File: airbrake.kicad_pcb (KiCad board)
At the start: 2 copper layers, 53.9 x 52.1 mm, 76 parts, among them IC1 SN74HCT125DR, J1 Molex Microfit, J2 Molex Microfit, J3 Molex Microfit, J4 Molex Microfit, J5 Molex Microfit, J6 Conn_02x03_Counter_Clockwise, U1 MS560702BA03-50, U2 MMC5983MA, U3 STM32G431RBTx, U4 TMP275AIDGKR, U5 LP5912Q3.3DRVRQ1, U6 BMI088, U7 TPS62153, U8 USBLC6-2SC6, U9 W25Q256JVEIQTR, X1 ECS-TXO-32CSMV-320-AN-TR

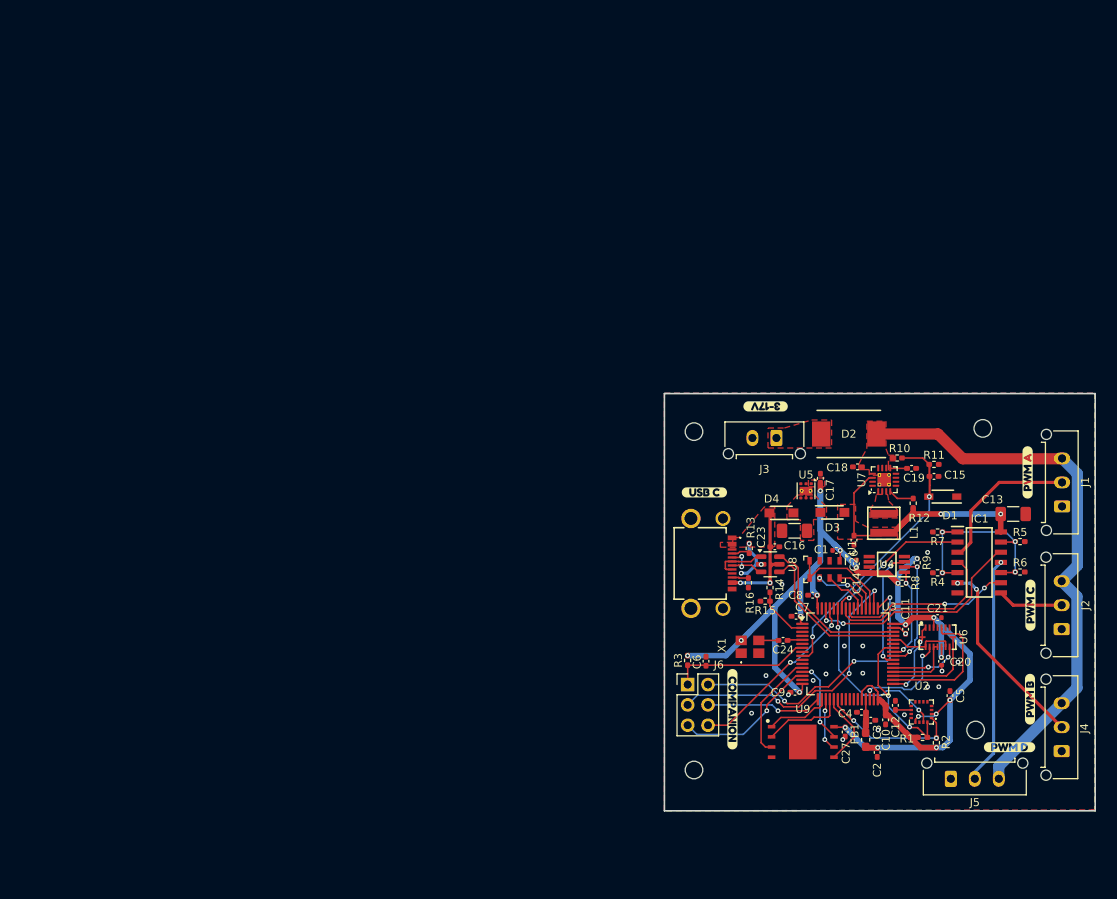
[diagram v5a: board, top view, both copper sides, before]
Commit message: feat: v2 schematic
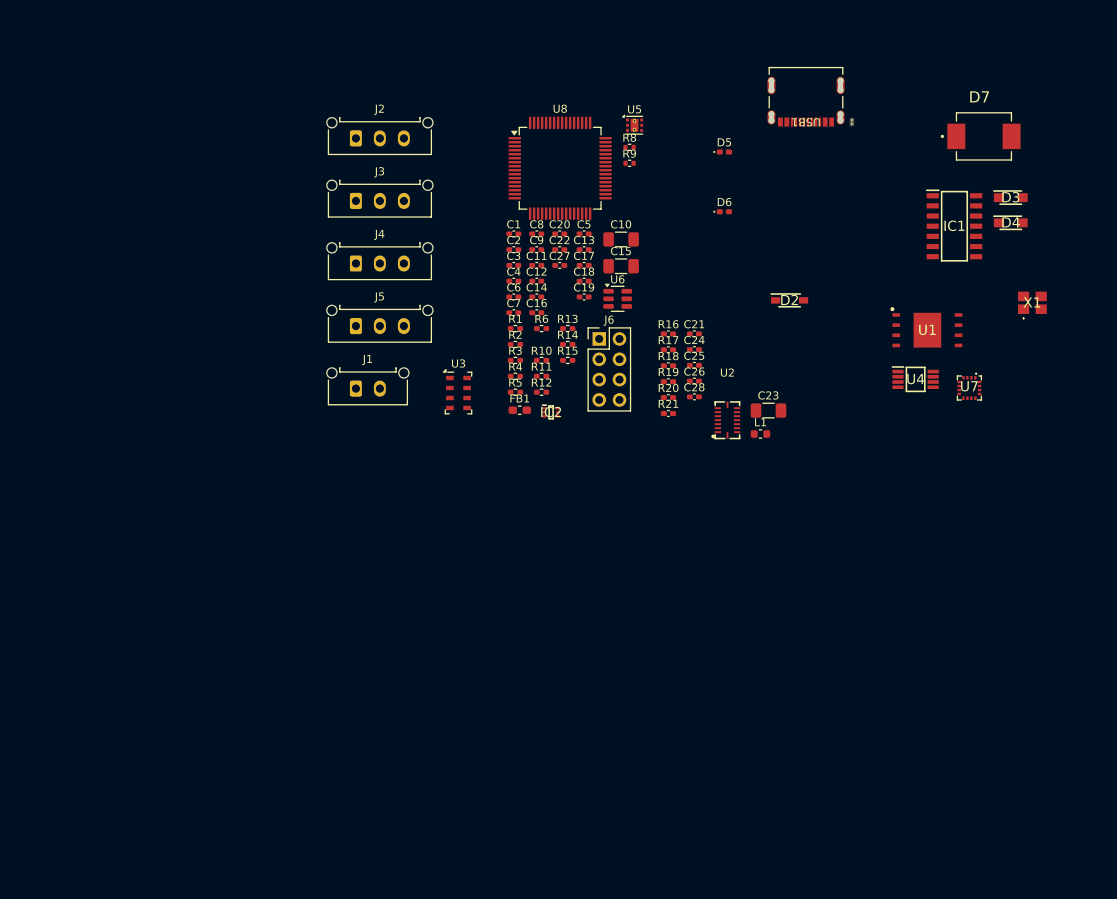
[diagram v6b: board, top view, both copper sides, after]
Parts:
- removed D1: MMSZ4683T1G, SamacSys:SOD3716X135N
- removed H1, H2, H3, H4: MountingHole, MountingHole:MountingHole_2.2mm_M2
- removed R7: 470R, Resistor_SMD:R_0402_1005Metric_Pad0.72x0.64mm_HandSolder
- removed U9: W25Q256JVEIQTR, SamacSys:SON127P800X600X80-9N-D
- removed kibuzzard-67AC9DCF: G***, kibuzzard-67AC9DCF
- removed kibuzzard-67AC9E05: G***, kibuzzard-67AC9E05
- removed kibuzzard-67AC9E3B: G***, kibuzzard-67AC9E3B
- removed kibuzzard-67AC9E4A: G***, kibuzzard-67AC9E4A
- removed kibuzzard-67AC9E5D: G***, kibuzzard-67AC9E5D
- removed kibuzzard-67AC9E80: G***, kibuzzard-67AC9E80
- removed kibuzzard-67B37024: G***, kibuzzard-67B37024
- added C22: 10uF, Capacitor_SMD:C_0402_1005Metric_Pad0.74x0.62mm_HandSolder, F.Cu at (110.6, 61.5)
- added C25: 10uF, Capacitor_SMD:C_0402_1005Metric_Pad0.74x0.62mm_HandSolder, F.Cu at (127.5, 75.9)
- added C28: 10nF, Capacitor_SMD:C_0402_1005Metric_Pad0.74x0.62mm_HandSolder, F.Cu at (127.5, 79.9)
- added D5: PWR_LED, LED_SMD:LED_0402_1005Metric_Pad0.77x0.64mm_HandSolder, F.Cu at (131.2, 49.2)
- added D6: USB_LED, LED_SMD:LED_0402_1005Metric_Pad0.77x0.64mm_HandSolder, F.Cu at (131.2, 56.7)
- added D7: SS34, footprints:DIOM7959X265N, F.Cu at (163.6, 47.3)
- added IC2: TPS563203DRLR, footprints:SOTFL50P160X60-6N, F.Cu at (109.5, 81.8)
- added R17: 10k, Inductor_SMD:L_0402_1005Metric_Pad0.77x0.64mm_HandSolder, F.Cu at (124.2, 74.0)
- added R18: 10k, Inductor_SMD:L_0402_1005Metric_Pad0.77x0.64mm_HandSolder, F.Cu at (124.2, 76.0)
- added R19: 22k, Inductor_SMD:L_0402_1005Metric_Pad0.77x0.64mm_HandSolder, F.Cu at (124.2, 78.0)
- added R20: 100k, Inductor_SMD:L_0402_1005Metric_Pad0.77x0.64mm_HandSolder, F.Cu at (124.2, 80.0)
- added R21: 100k, Inductor_SMD:L_0402_1005Metric_Pad0.77x0.64mm_HandSolder, F.Cu at (124.2, 81.9)
- C1, C14, C20: footprint Capacitor_SMD:C_0402_1005Metric -> Capacitor_SMD:C_0402_1005Metric_Pad0.74x0.62mm_HandSolder
- C10, C15: value 100nF -> 100uF; footprint Capacitor_SMD:C_0402_1005Metric_Pad0.74x0.62mm_HandSolder -> Capacitor_SMD:C_1206_3216Metric_Pad1.33x1.80mm_HandSolder
- C12: value 10uF -> 100nF
- C13: value 100uF -> 100nF; footprint Capacitor_SMD:C_1206_3216Metric_Pad1.33x1.80mm_HandSolder -> Capacitor_SMD:C_0402_1005Metric_Pad0.74x0.62mm_HandSolder
- C16: value 100uF -> 1uF; footprint Capacitor_SMD:C_1206_3216Metric_Pad1.33x1.80mm_HandSolder -> Capacitor_SMD:C_0402_1005Metric_Pad0.74x0.62mm_HandSolder
- C17: value 2.2uF -> 10uF
- C18: value 10uF -> 2.2uF
- C19: value 3.3pF -> 10nF
- C21: value 100nF -> 22uF; footprint Capacitor_SMD:C_0402_1005Metric -> Capacitor_SMD:C_0402_1005Metric_Pad0.74x0.62mm_HandSolder
- C23: value 10uF -> 100uF; footprint Capacitor_SMD:C_0402_1005Metric_Pad0.74x0.62mm_HandSolder -> Capacitor_SMD:C_1206_3216Metric_Pad1.33x1.80mm_HandSolder
- C24: value 10nF -> 22uF
- C26: value 22uF -> 100nF
- C3: value 10nF -> 100nF
- C4, C5: value 1uF -> 100nF
- C6: value 100nF -> 10nF
- C8: value 100nF -> 1uF
- D2: value SS34 -> MMSZ4683T1G; footprint SamacSys:DIOM7959X262N -> footprints:SOD3716X135N
- D3, D4: footprint SamacSys:SODFL3616X98N -> footprints:SODFL3616X98N
- IC1: footprint SamacSys:SOIC127P600X175-14N -> footprints:SOIC127P600X175-14N
- J1: footprint Connector_Molex:Molex_Micro-Fit_3.0_43650-0315_1x03_P3.00mm_Vertical -> Connector_Molex:Molex_Micro-Fit_3.0_43650-0215_1x02_P3.00mm_Vertical
- J3: footprint Connector_Molex:Molex_Micro-Fit_3.0_43650-0215_1x02_P3.00mm_Vertical -> Connector_Molex:Molex_Micro-Fit_3.0_43650-0315_1x03_P3.00mm_Vertical
- J6: footprint Connector_PinHeader_2.54mm:PinHeader_2x03_P2.54mm_Vertical -> Connector_PinHeader_2.54mm:PinHeader_2x04_P2.54mm_Vertical
- L1: value 2.2uH -> 4.7uH; footprint SamacSys:XFL4020472MEC -> Inductor_SMD:L_0603_1608Metric
- R1: value 4.7k -> 10k
- R10, R14: value 10k -> 4.7k
- R11: value 47k -> 5.1k
- R12: value 100k -> 10k
- R13: value 5.1k -> 22k
- R15: value 22k -> 10k
- R16: value 5.1k -> 100k; footprint Resistor_SMD:R_0402_1005Metric_Pad0.72x0.64mm_HandSolder -> Inductor_SMD:L_0402_1005Metric_Pad0.77x0.64mm_HandSolder
- R2: value 4.7k -> 47k
- R3: value 10k -> 470R
- U1: value MS560702BA03-50 -> W25Q256JVEIQTR; footprint Package_LGA:LGA-8_3x5mm_P1.25mm -> footprints:SON127P800X600X80-9N-D
- U2: value MMC5983MA -> BMI088; footprint SamacSys:MMC5983MA -> footprints:LGA-16_L4.5-W3.0-P0.50-BL
- U3: value STM32G431RBTx -> MS560702BA03-50; footprint Package_QFP:LQFP-64_10x10mm_P0.5mm -> Package_LGA:LGA-8_3x5mm_P1.25mm
- U4: footprint SamacSys:SOP65P490X110-8N -> footprints:SOP65P490X110-8N
- U6: value BMI088 -> USBLC6-2SC6; footprint EasyEDA:LGA-16_L4.5-W3.0-P0.50-BL -> Package_TO_SOT_SMD:SOT-23-6
- U7: value TPS62153 -> MMC5983MA; footprint Package_DFN_QFN:VQFN-16-1EP_3x3mm_P0.5mm_EP1.68x1.68mm_ThermalVias -> footprints:MMC5983MA
- U8: value USBLC6-2SC6 -> STM32G431RBTx; footprint Package_TO_SOT_SMD:SOT-23-6 -> Package_QFP:LQFP-64_10x10mm_P0.5mm
- USB1: value 10172013-00011LF -> 2137160001; footprint SamacSys:1017201300011LF -> footprints:2171790001_MOL
- X1: footprint SamacSys:ECSTXO32CSMV320ANTR -> footprints:ECSTXO32CSMV320ANTR
- moved J2 107.5 mm to (85.1, 47.5), turned to 0 degrees
- moved J4 107.2 mm to (85.1, 63.2), turned to 0 degrees
- moved J5 93.4 mm to (85.1, 71.0)
- moved J1 89.5 mm to (85.1, 78.8), turned to 0 degrees
- moved C2 77.5 mm to (104.9, 61.5), turned to 0 degrees
- moved C5 73.6 mm to (113.7, 59.5), turned to 0 degrees
- moved R2 72.4 mm to (105.1, 73.3), turned to 0 degrees
- moved C3 72.3 mm to (104.9, 63.4)
- moved R1 72.1 mm to (105.1, 71.3), turned to 0 degrees
- moved C20 71.6 mm to (110.6, 59.5), turned to 0 degrees
- moved C12 69.4 mm to (107.7, 65.4), turned to 0 degrees
- moved C4 69.2 mm to (104.9, 65.4), turned to 0 degrees
- moved C10 68.6 mm to (118.3, 60.2), turned to 0 degrees
- moved C27 68.4 mm to (110.6, 63.4), turned to 0 degrees
- moved R6 67.1 mm to (108.3, 71.3)
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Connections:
- C1 pad 1: VBAT- -> +3.3V
- C1 pad 2: +3.3V -> VBAT-
- C10 pad 1: +3.3V -> 6V0
- C12 pad 1: Net-(U2-CAP) -> +3.3V
- C13 pad 1: +5V -> +3.3V
- C15 pad 1: VBAT- -> Net-(D3-K)
- C15 pad 2: BAT_LEVEL -> VBAT-
- C16 pad 1: Net-(D3-K) -> VBAT-
- C16 pad 2: VBAT- -> +3.3V
- C17 pad 2: +3.3V -> VBUS
- C18 pad 2: VBAT+ -> +3.3V
- C19 pad 1: VBAT- -> HSE_IN
- C19 pad 2: Net-(U7-SS/TR) -> Net-(X1-OUTPUT)
- C20 pad 1: +3.3V -> VBAT-
- C20 pad 2: VBAT- -> +3.3V
- C21 pad 1: +3.3V -> 6V0
- C23 pad 1: VBAT- -> VBAT+
- C23 pad 2: VBUS -> VBAT-
- C24 pad 1: HSE_IN -> 6V0
- C24 pad 2: Net-(X1-OUTPUT) -> VBAT-
- C26 pad 1: VBAT- -> Net-(IC2-SW)
- C26 pad 2: +5V -> Net-(IC2-BST)
- C27 pad 1: +3.3V -> VBAT-
- C27 pad 2: VBAT- -> nRST
- C3 pad 1: +3.3VA -> +3.3V
- C4 pad 1: +3.3VA -> +3.3V
- C5 pad 2: +3.3V -> BAT_LEVEL
- C6 pad 1: VBAT- -> +3.3VA
- C6 pad 2: nRST -> VBAT-
- C8 pad 1: +3.3V -> +3.3VA
- D2 pad 1: VBAT+ -> VBAT-
- D2 pad 2: Net-(D2-A) -> BAT_LEVEL
- D3 pad 2: +5V -> 6V0
- IC1 pad 14: +5V -> 6V0
- J1 pad 1: VBAT- -> Net-(J1-Pin_1)
- J1 pad 2: SERVO_A -> VBAT-
- J2 pad 2: SERVO_C -> SERVO_A
- J2 pad 3: VBAT+ -> 6V0
- J3 pad 1: Net-(D2-A) -> VBAT-
- J3 pad 2: VBAT- -> SERVO_B
- J4 pad 2: SERVO_B -> SERVO_C
- J4 pad 3: VBAT+ -> 6V0
- J5 pad 3: VBAT+ -> 6V0
- J6 pad 1: nRST -> VBAT-
- J6 pad 4: COMPANION_RX -> +3.3V
- J6 pad 5: COMPANION_TX -> COMPANION_RX
- J6 pad 6: BOOT0 -> COMPANION_TX
- L1 pad 1: +5V -> 6V0
- L1 pad 2: Net-(L1-Pad2) -> Net-(IC2-SW)
- R1 pad 1: MMC5983MA_SDA -> VBAT+
- R1 pad 2: +3.3V -> BAT_LEVEL
- R10 pad 1: VBAT+ -> +3.3V
- R10 pad 2: BAT_LEVEL -> MMC5983MA_SCL
- R11 pad 1: BAT_LEVEL -> unconnected-(R11-Pad1)
- R11 pad 2: VBAT- -> Net-(USB1-CC2)
- R12 pad 1: +5V -> VBUS
- R12 pad 2: Net-(U7-PG) -> BCD
- R13 pad 1: VBAT- -> BCD
- R13 pad 2: Net-(USB1-CC1) -> VBAT-
- R14 pad 1: VBUS -> MMC5983MA_SDA
- R14 pad 2: BCD -> +3.3V
- R15 pad 1: BCD -> nRST
- R15 pad 2: VBAT- -> +3.3V
- R16 pad 1: Net-(USB1-CC2) -> Net-(IC2-FB)
- R2 pad 1: +3.3V -> BAT_LEVEL
- R2 pad 2: MMC5983MA_SCL -> VBAT-
- R3 pad 1: nRST -> /PWM_PD
- R3 pad 2: +3.3V -> VBAT-
- U1 pad 1: +3.3V -> W25Q_NSS
- U1 pad 2: VBAT- -> W25Q_MISO
- U1 pad 3: VBAT- -> W25Q_WP
- U1 pad 4: MS5607_NSS -> VBAT-
- U1 pad 5: MS5607_NSS -> W25Q_MOSI
- U1 pad 6: MS5607_MISO -> W25Q_SCK
- U1 pad 7: MS5607_MOSI -> W25Q_HOLD
- U1 pad 8: MS5607_SCLK -> +3.3V
- U2 pad 1: MMC5983MA_SCL -> BMI088_ACCEL_INT
- U2 pad 10: Net-(U2-CAP) -> BMI088_MISO
- U2 pad 11: VBAT- -> +3.3V
- U2 pad 12: unconnected-(U2-NC-Pad12) -> BMI088_GYRO_INT
- U2 pad 13: +3.3V -> BMI088_GYRO_INT
- U2 pad 14: unconnected-(U2-NC-Pad14) -> BMI088_ACCEL_CS
- U2 pad 15: MMC5983MA_INT -> BMI088_MISO
- U2 pad 16: MMC5983MA_SDA -> BMI088_ACCEL_INT
- U2 pad 2: +3.3V -> VBAT-
- U2 pad 3: unconnected-(U2-NC-Pad3) -> +3.3V
- U2 pad 4: unconnected-(U2-SPI_CS-Pad4) -> VBAT-
- U2 pad 5: unconnected-(U2-SPI_SDO-Pad5) -> BMI088_GYRO_CS
- U2 pad 6: unconnected-(U2-NC-Pad6) -> VBAT-
- U2 pad 7: unconnected-(U2-NC-Pad7) -> VBAT-
- U2 pad 8: unconnected-(U2-NC-Pad8) -> BMI088_SCLK
- U2 pad 9: VBAT- -> BMI088_MOSI
- U3 pad 2: BCD -> VBAT-
- U3 pad 3: unconnected-(U3-PC14-Pad3) -> VBAT-
- U3 pad 4: unconnected-(U3-PC15-Pad4) -> MS5607_NSS
- U3 pad 5: HSE_IN -> MS5607_NSS
- U3 pad 6: unconnected-(U3-PF1-Pad6) -> MS5607_MISO
- U3 pad 7: nRST -> MS5607_MOSI
- U3 pad 8: unconnected-(U3-PC0-Pad8) -> MS5607_SCLK
- U6 pad 1: BMI088_ACCEL_INT -> D+
- U6 pad 3: +3.3V -> D-
- U6 pad 4: VBAT- -> USB_DN
- U6 pad 5: BMI088_GYRO_CS -> VBUS
- U6 pad 6: VBAT- -> USB_DP
- U7 pad 1: Net-(L1-Pad2) -> MMC5983MA_SCL
- U7 pad 10: VBAT+ -> Net-(U7-CAP)
- U7 pad 11: VBAT+ -> VBAT-
- U7 pad 12: VBAT+ -> unconnected-(U7-NC-Pad12)
- U7 pad 13: VBAT+ -> +3.3V
- U7 pad 14: +5V -> unconnected-(U7-NC-Pad14)
- U7 pad 15: VBAT- -> MMC5983MA_INT
- U7 pad 16: VBAT- -> MMC5983MA_SDA
- U7 pad 2: Net-(L1-Pad2) -> +3.3V
- U7 pad 3: Net-(L1-Pad2) -> unconnected-(U7-NC-Pad3)
- U7 pad 4: Net-(U7-PG) -> unconnected-(U7-SPI_CS-Pad4)
- U7 pad 5: VBAT- -> unconnected-(U7-SPI_SDO-Pad5)
- U7 pad 6: VBAT- -> unconnected-(U7-NC-Pad6)
- U7 pad 7: VBAT- -> unconnected-(U7-NC-Pad7)
- U7 pad 8: VBAT- -> unconnected-(U7-NC-Pad8)
- U7 pad 9: Net-(U7-SS/TR) -> VBAT-
- U8 pad 1: D+ -> +3.3V
- U8 pad 2: VBAT- -> BCD
- U8 pad 3: D- -> unconnected-(U8-PC14-Pad3)
- U8 pad 4: USB_DN -> unconnected-(U8-PC15-Pad4)
- U8 pad 5: VBUS -> HSE_IN
- U8 pad 6: USB_DP -> unconnected-(U8-PF1-Pad6)
- USB1 pad A5: Net-(USB1-CC1) -> VBAT-
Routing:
- net +3.3V: track 166.0 -> 0.00 mm, vias 19 -> 0
- net VBAT+: track 71.0 -> 0.00 mm
- net BAT_LEVEL: track 38.5 -> 0.00 mm, vias 2 -> 0
- net SWCLK: track 36.9 -> 0.00 mm, vias 3 -> 0
- net SWDIO: track 35.8 -> 0.00 mm, vias 3 -> 0
- net +5V: track 32.1 -> 0.00 mm, vias 2 -> 0
- net SERVO_D: track 28.4 -> 0.00 mm, vias 1 -> 0
- net PWM_D: track 28.2 -> 0.00 mm, vias 2 -> 0
- net /PWM_PD: track 25.7 -> 0.00 mm, vias 4 -> 0
- net SERVO_B: track 24.3 -> 0.00 mm, vias 2 -> 0
- net BOOT0: track 22.8 -> 0.00 mm, vias 2 -> 0
- net PWM_B: track 22.1 -> 0.00 mm
- net MMC5983MA_INT: track 22.0 -> 0.00 mm, vias 2 -> 0
- net PWM_C: track 21.6 -> 0.00 mm, vias 2 -> 0
- net USB_DP: track 20.1 -> 0.00 mm
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- removed copper zone on F.Cu, net +3.3V
- removed copper zone on F.Cu, net +5V
- removed copper zone on F.Cu, net Net-(D2-A)
- removed copper zone on F.Cu, net Net-(D3-K)
- removed copper zone on F.Cu, net Net-(L1-Pad2)
- removed copper zone on F.Cu, net VBAT+
- removed copper zone on B.Cu, net VBAT-
- removed copper zone on F.Cu, net VBAT-
- removed copper zone on F.Cu, net VBUS
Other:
- board size 53.9 x 52.1 mm -> 8.6 x 5 mm

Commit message: feat: v3
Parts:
- removed D7: SS34, footprints:DIOM7959X265N
- added D1: NRVB120VLSFT1G, footprints:SODFL3616X98N, F.Cu at (139.6, 96.6)
- added H1: MH, PCM_SL_Mechanical:MountingHole_3.2mm_Pad, F.Cu at (172.2, 134.8)
- added H2: MH, PCM_SL_Mechanical:MountingHole_3.2mm_Pad, F.Cu at (172.4, 80.8)
- added H3: MH, PCM_SL_Mechanical:MountingHole_3.2mm_Pad, F.Cu at (120.2, 80.8)
- added H4: MH, PCM_SL_Mechanical:MountingHole_3.2mm_Pad, F.Cu at (120.2, 134.8)
- added R22: 5.1k, Resistor_SMD:R_0402_1005Metric_Pad0.72x0.64mm_HandSolder, F.Cu at (128.2, 108.3)
- added R23: 5.1k, Resistor_SMD:R_0402_1005Metric_Pad0.72x0.64mm_HandSolder, F.Cu at (128.9, 112.5)
- added R7: 470R, Resistor_SMD:R_0402_1005Metric_Pad0.72x0.64mm_HandSolder, F.Cu at (154.2, 106.1)
- added kibuzzard-682EDA3B: G***, kibuzzard-682EDA3B, F.Cu at (163.2, 82.5)
- added kibuzzard-682EDA42: G***, kibuzzard-682EDA42, F.Cu at (147.9, 82.5)
- added kibuzzard-682EDA9B: G***, kibuzzard-682EDA9B, F.Cu at (167.3, 109.0)
- added kibuzzard-682EDAA9: G***, kibuzzard-682EDAA9, F.Cu at (167.3, 123.6)
- added kibuzzard-682EDAC6: G***, kibuzzard-682EDAC6, F.Cu at (117.6, 90.2)
- added kibuzzard-682EDAD5: G***, kibuzzard-682EDAD5, F.Cu at (117.9, 110.3)
- added kibuzzard-682EDAED: G***, kibuzzard-682EDAED, F.Cu at (117.8, 123.7)
- added kibuzzard-682EDBD7: G***, kibuzzard-682EDBD7, B.Cu at (160.8, 136.9)
- added kibuzzard-682EDEAD: G***, kibuzzard-682EDEAD, B.Cu at (145.7, 108.8)
- added kibuzzard-682EDEC5: G***, kibuzzard-682EDEC5, B.Cu at (145.6, 105.7)
- C10, C15, C23: value 100uF -> 100nF; footprint Capacitor_SMD:C_1206_3216Metric_Pad1.33x1.80mm_HandSolder -> Capacitor_SMD:C_0402_1005Metric_Pad0.74x0.62mm_HandSolder
- C12, C20: value 100nF -> 10uF
- C13: value 100nF -> 100uF; footprint Capacitor_SMD:C_0402_1005Metric_Pad0.74x0.62mm_HandSolder -> Capacitor_SMD:C_1206_3216Metric_Pad1.33x1.80mm_HandSolder
- C16: value 1uF -> 2.2uF
- C17: value 10uF -> 100uF; footprint Capacitor_SMD:C_0402_1005Metric_Pad0.74x0.62mm_HandSolder -> Capacitor_SMD:C_1206_3216Metric_Pad1.33x1.80mm_HandSolder
- C18: value 2.2uF -> 10nF
- C19: value 10nF -> 100uF; footprint Capacitor_SMD:C_0402_1005Metric_Pad0.74x0.62mm_HandSolder -> Capacitor_SMD:C_1206_3216Metric_Pad1.33x1.80mm_HandSolder
- C21: value 22uF -> 10nF
- C24: value 22uF -> 100nF
- C25: value 10uF -> 100nF
- C26, C27: value 100nF -> 22uF
- C28, C6: value 10nF -> 100nF
- C3: value 100nF -> 10nF
- C4, C5: value 100nF -> 1uF
- C8: value 1uF -> 100nF
- D4: value NRVB120VLSFT1G -> SS34; footprint footprints:SODFL3616X98N -> footprints:DIOM7959X265N
- J1: footprint Connector_Molex:Molex_Micro-Fit_3.0_43650-0215_1x02_P3.00mm_Vertical -> Connector_Molex:Molex_Micro-Fit_3.0_43650-0315_1x03_P3.00mm_Vertical
- J5: value Molex Microfit -> Conn_02x03_Counter_Clockwise; footprint Connector_Molex:Molex_Micro-Fit_3.0_43650-0315_1x03_P3.00mm_Vertical -> Connector_PinHeader_2.54mm:PinHeader_2x04_P2.54mm_Vertical
- J6: value Conn_02x03_Counter_Clockwise -> Molex Microfit; footprint Connector_PinHeader_2.54mm:PinHeader_2x04_P2.54mm_Vertical -> Connector_Molex:Molex_Micro-Fit_3.0_43650-0215_1x02_P3.00mm_Vertical
- L1: footprint Inductor_SMD:L_0603_1608Metric -> footprints:INDPM5050X400N
- R1: value 10k -> 4.7k
- R10: value 4.7k -> 10k
- R11: value 5.1k -> 10k
- R12: value 10k -> 47k
- R13: value 22k -> 100k; footprint Resistor_SMD:R_0402_1005Metric_Pad0.72x0.64mm_HandSolder -> Inductor_SMD:L_0402_1005Metric_Pad0.77x0.64mm_HandSolder
- R14: value 4.7k -> 100k; footprint Resistor_SMD:R_0402_1005Metric_Pad0.72x0.64mm_HandSolder -> Inductor_SMD:L_0402_1005Metric_Pad0.77x0.64mm_HandSolder
- R15: footprint Resistor_SMD:R_0402_1005Metric_Pad0.72x0.64mm_HandSolder -> Inductor_SMD:L_0402_1005Metric_Pad0.77x0.64mm_HandSolder
- R18: value 10k -> 22k
- R19: value 22k -> 22R; footprint Inductor_SMD:L_0402_1005Metric_Pad0.77x0.64mm_HandSolder -> Resistor_SMD:R_0402_1005Metric_Pad0.72x0.64mm_HandSolder
- R2: value 47k -> 4.7k
- R20: value 100k -> 22R; footprint Inductor_SMD:L_0402_1005Metric_Pad0.77x0.64mm_HandSolder -> Resistor_SMD:R_0402_1005Metric_Pad0.72x0.64mm_HandSolder
- R21: value 100k -> 1.5k; footprint Inductor_SMD:L_0402_1005Metric_Pad0.77x0.64mm_HandSolder -> Resistor_SMD:R_0402_1005Metric_Pad0.72x0.64mm_HandSolder
- R3: value 470R -> 10k
- U1: value W25Q256JVEIQTR -> MS560702BA03-50; footprint footprints:SON127P800X600X80-9N-D -> Package_LGA:LGA-8_3x5mm_P1.25mm
- U2: value BMI088 -> MMC5983MA; footprint footprints:LGA-16_L4.5-W3.0-P0.50-BL -> footprints:MMC5983MA
- U3: value MS560702BA03-50 -> STM32G431RBTx; footprint Package_LGA:LGA-8_3x5mm_P1.25mm -> Package_QFP:LQFP-64_10x10mm_P0.5mm
- U6: value USBLC6-2SC6 -> BMI088; footprint Package_TO_SOT_SMD:SOT-23-6 -> footprints:LGA-16_L4.5-W3.0-P0.50-BL
- U7: value MMC5983MA -> USBLC6-2SC6; footprint footprints:MMC5983MA -> Package_TO_SOT_SMD:SOT-23-6
- U8: value STM32G431RBTx -> W25Q256JVEIQTR; footprint Package_QFP:LQFP-64_10x10mm_P0.5mm -> footprints:SON127P800X600X80-9N-D
- moved J2 108.2 mm to (171.9, 112.1), turned to 90 degrees
- moved J4 107.5 mm to (172.0, 126.6), turned to 90 degrees
- moved J3 89.3 mm to (168.2, 88.0), turned to 180 degrees
- moved R8 83.8 mm to (146.9, 127.8), turned to -90 degrees
- moved C3 82.6 mm to (153.9, 129.9)
- moved C8 82.5 mm to (155.5, 126.7), turned to -90 degrees
- moved U8 80.7 mm to (137.1, 127.5), turned to 180 degrees
- moved C4 79.9 mm to (153.9, 128.4)
- moved R9 79.5 mm to (144.3, 126.1)
- moved C12 79.1 mm to (162.8, 122.1)
- moved C11 77.3 mm to (151.2, 127.4), turned to 180 degrees
- moved C14 76.5 mm to (147.7, 132.6), turned to 180 degrees
- moved R1 74.7 mm to (164.0, 117.3), turned to 90 degrees
- moved C2 73.7 mm to (143.1, 124.5), turned to -90 degrees
- moved C9 73.5 mm to (158.0, 115.0)
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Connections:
- C1 pad 1: +3.3V -> VBAT-
- C1 pad 2: VBAT- -> +3.3V
- C10 pad 1: 6V0 -> +3.3V
- C12 pad 1: +3.3V -> Net-(U2-CAP)
- C13 pad 1: +3.3V -> 6V0
- C15 pad 1: Net-(D3-K) -> VBAT-
- C15 pad 2: VBAT- -> BAT_LEVEL
- C17 pad 1: VBAT- -> Net-(D1-K)
- C17 pad 2: VBUS -> VBAT-
- C18 pad 1: VBAT- -> HSE_IN
- C18 pad 2: +3.3V -> Net-(X1-OUTPUT)
- C19 pad 1: HSE_IN -> VBAT+
- C19 pad 2: Net-(X1-OUTPUT) -> VBAT-
- C20 pad 1: VBAT- -> VBAT+
- C20 pad 2: +3.3V -> VBAT-
- C21 pad 1: 6V0 -> Net-(IC2-EN)
- C22 pad 1: Net-(U7-CAP) -> VBAT-
- C22 pad 2: VBAT- -> VBUS
- C23 pad 1: VBAT+ -> +3.3V
- C24 pad 1: 6V0 -> +3.3V
- C25 pad 1: VBAT+ -> Net-(IC2-SW)
- C25 pad 2: VBAT- -> Net-(IC2-BST)
- C26 pad 1: Net-(IC2-SW) -> 6V0
- C26 pad 2: Net-(IC2-BST) -> VBAT-
- C27 pad 1: VBAT- -> 6V0
- C27 pad 2: nRST -> VBAT-
- C28 pad 1: Net-(IC2-EN) -> +3.3V
- C3 pad 1: +3.3V -> +3.3VA
- C4 pad 1: +3.3V -> +3.3VA
- C5 pad 2: BAT_LEVEL -> +3.3V
- C6 pad 1: +3.3VA -> VBAT-
- C6 pad 2: VBAT- -> nRST
- C8 pad 1: +3.3VA -> +3.3V
- D3 pad 1: Net-(D3-K) -> Net-(D1-K)
- D3 pad 2: 6V0 -> VBUS
- J1 pad 1: Net-(J1-Pin_1) -> VBAT-
- J1 pad 2: VBAT- -> SERVO_A
- J2 pad 2: SERVO_A -> SERVO_C
- J4 pad 2: SERVO_C -> SERVO_D
- J5 pad 2: SERVO_D -> SWDIO
- J5 pad 3: 6V0 -> SWCLK
- J6 pad 1: VBAT- -> Net-(J6-Pin_1)
- J6 pad 2: SWDIO -> VBAT-
- R1 pad 1: VBAT+ -> MMC5983MA_SDA
- R1 pad 2: BAT_LEVEL -> +3.3V
- R10 pad 1: +3.3V -> Net-(U3-PC13)
- R10 pad 2: MMC5983MA_SCL -> BCD
- R11 pad 1: unconnected-(R11-Pad1) -> VBAT+
- R11 pad 2: Net-(USB1-CC2) -> BAT_LEVEL
- R12 pad 1: VBUS -> BAT_LEVEL
- R12 pad 2: BCD -> VBAT-
- R13 pad 1: BCD -> Net-(D5-Pad1)
- R14 pad 1: MMC5983MA_SDA -> Net-(D6-Pad1)
- R14 pad 2: +3.3V -> VBAT-
- R15 pad 1: nRST -> Net-(IC2-FB)
- R15 pad 2: +3.3V -> 6V0
- R17 pad 1: Net-(IC2-FB) -> VBAT-
- R17 pad 2: 6V0 -> Net-(IC2-EN)
- R18 pad 1: VBAT- -> Net-(IC2-EN)
- R18 pad 2: Net-(IC2-EN) -> VBAT+
- R19 pad 1: Net-(IC2-EN) -> Net-(R19-Pad1)
- R19 pad 2: VBAT+ -> D+
- R2 pad 1: BAT_LEVEL -> +3.3V
- R2 pad 2: VBAT- -> MMC5983MA_SCL
- R20 pad 1: Net-(D6-Pad1) -> Net-(R20-Pad1)
- R20 pad 2: VBAT- -> D-
- R21 pad 1: Net-(D5-Pad1) -> D+
- R21 pad 2: VBAT- -> +3.3V
- R3 pad 1: /PWM_PD -> nRST
- R3 pad 2: VBAT- -> +3.3V
- U1 pad 1: W25Q_NSS -> +3.3V
- U1 pad 2: W25Q_MISO -> VBAT-
- U1 pad 3: W25Q_WP -> VBAT-
- U1 pad 4: VBAT- -> MS5607_NSS
- U1 pad 5: W25Q_MOSI -> MS5607_NSS
- U1 pad 6: W25Q_SCK -> MS5607_MISO
- U1 pad 7: W25Q_HOLD -> MS5607_MOSI
- U1 pad 8: +3.3V -> MS5607_SCLK
- U2 pad 1: BMI088_ACCEL_INT -> MMC5983MA_SCL
- U2 pad 10: BMI088_MISO -> Net-(U2-CAP)
- U2 pad 11: +3.3V -> VBAT-
- U2 pad 12: BMI088_GYRO_INT -> unconnected-(U2-NC-Pad12)
- U2 pad 13: BMI088_GYRO_INT -> +3.3V
- U2 pad 14: BMI088_ACCEL_CS -> unconnected-(U2-NC-Pad14)
- U2 pad 15: BMI088_MISO -> MMC5983MA_INT
- U2 pad 16: BMI088_ACCEL_INT -> MMC5983MA_SDA
- U2 pad 2: VBAT- -> +3.3V
- U2 pad 3: +3.3V -> unconnected-(U2-NC-Pad3)
- U2 pad 4: VBAT- -> unconnected-(U2-SPI_CS-Pad4)
- U2 pad 5: BMI088_GYRO_CS -> unconnected-(U2-SPI_SDO-Pad5)
- U2 pad 6: VBAT- -> unconnected-(U2-NC-Pad6)
- U2 pad 7: VBAT- -> unconnected-(U2-NC-Pad7)
- U2 pad 8: BMI088_SCLK -> unconnected-(U2-NC-Pad8)
- U2 pad 9: BMI088_MOSI -> VBAT-
- U3 pad 2: VBAT- -> Net-(U3-PC13)
- U3 pad 3: VBAT- -> unconnected-(U3-PC14-Pad3)
- U3 pad 4: MS5607_NSS -> unconnected-(U3-PC15-Pad4)
- U3 pad 5: MS5607_NSS -> HSE_IN
- U3 pad 6: MS5607_MISO -> unconnected-(U3-PF1-Pad6)
- U3 pad 7: MS5607_MOSI -> nRST
- U3 pad 8: MS5607_SCLK -> unconnected-(U3-PC0-Pad8)
- U5 pad 4: Net-(D3-K) -> Net-(D1-K)
- U5 pad 6: Net-(D3-K) -> Net-(D1-K)
- U6 pad 1: D+ -> BMI088_ACCEL_INT
- U6 pad 3: D- -> +3.3V
- U6 pad 4: USB_DN -> VBAT-
- U6 pad 5: VBUS -> BMI088_GYRO_CS
- U6 pad 6: USB_DP -> VBAT-
- U7 pad 1: MMC5983MA_SCL -> Net-(R19-Pad1)
- U7 pad 2: +3.3V -> VBAT-
- U7 pad 3: unconnected-(U7-NC-Pad3) -> Net-(R20-Pad1)
- U7 pad 4: unconnected-(U7-SPI_CS-Pad4) -> USB_DN
- U7 pad 5: unconnected-(U7-SPI_SDO-Pad5) -> VBUS
- U7 pad 6: unconnected-(U7-NC-Pad6) -> USB_DP
- U8 pad 1: +3.3V -> W25Q_NSS
- U8 pad 2: BCD -> W25Q_MISO
- U8 pad 3: unconnected-(U8-PC14-Pad3) -> W25Q_WP
- U8 pad 4: unconnected-(U8-PC15-Pad4) -> VBAT-
- U8 pad 5: HSE_IN -> W25Q_MOSI
- U8 pad 6: unconnected-(U8-PF1-Pad6) -> W25Q_SCK
- U8 pad 7: nRST -> W25Q_HOLD
- U8 pad 8: unconnected-(U8-PC0-Pad8) -> +3.3V
- U8 pad 9: BAT_LEVEL -> unconnected-(U8-EP-Pad9)
- USB1 pad A5: VBAT- -> BCD
- USB1 pad B5: Net-(USB1-CC2) -> BCD
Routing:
- net SWCLK: track 0.00 -> 37.1 mm, vias 0 -> 1
- net BOOT0: track 0.00 -> 36.5 mm, vias 0 -> 1
- net SWDIO: track 0.00 -> 36.2 mm, vias 0 -> 1
- net COMPANION_RX: track 0.00 -> 35.1 mm, vias 0 -> 1
- net +3.3V: track 0.00 -> 31.0 mm, vias 0 -> 22
- net VBUS: track 0.00 -> 30.0 mm
- net COMPANION_TX: track 0.00 -> 26.5 mm, vias 0 -> 1
- net nRST: track 0.00 -> 25.8 mm
- net SERVO_D: track 0.00 -> 25.1 mm, vias 0 -> 1
- net USB_DP: track 0.00 -> 24.4 mm
- net USB_DN: track 0.00 -> 24.4 mm
- net /PWM_PD: track 0.00 -> 24.3 mm, vias 0 -> 2
- net VBAT-: track 0.00 -> 22.6 mm, vias 0 -> 49
- net W25Q_MOSI: track 0.00 -> 22.1 mm, vias 0 -> 2
- net BCD: track 0.00 -> 21.9 mm, vias 0 -> 2
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- added copper zone on In2.Cu, net +3.3V
- added copper zone on F.Cu, net 6V0
- added copper zone on In2.Cu, net 6V0
- added copper zone on B.Cu, net VBAT+
- added copper zone on F.Cu, net VBAT-
- added copper zone on In1.Cu, net VBAT-
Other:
- board size 8.6 x 5 mm -> 61 x 63 mm
- copper layers 2 -> 4
